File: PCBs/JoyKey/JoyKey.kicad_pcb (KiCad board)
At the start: 2 copper layers, 97 x 56.8 mm, 50 parts, among them J1 OLED_DISPLAY, J2 Conn_01x03_Socket, J3 Testpad wire hole1, J4 JST PH, J5 Top Trigger 1, J6 Top Trigger 2, Q1 PMOS,Si7157DP, SW1 RotaryEncoder_Switch, SW2 SW_Push_45deg, SW3 SW_Push_45deg, SW4 SW_Push_45deg, SW5 SW_Push_45deg, SW6 SW_Push_45deg, SW7 SW_Push_45deg, U1 BQ25060, U3 XIAO-RP2040-DIP, U4 LP2981-3.3, U5 2_axis_analog_joystick_button

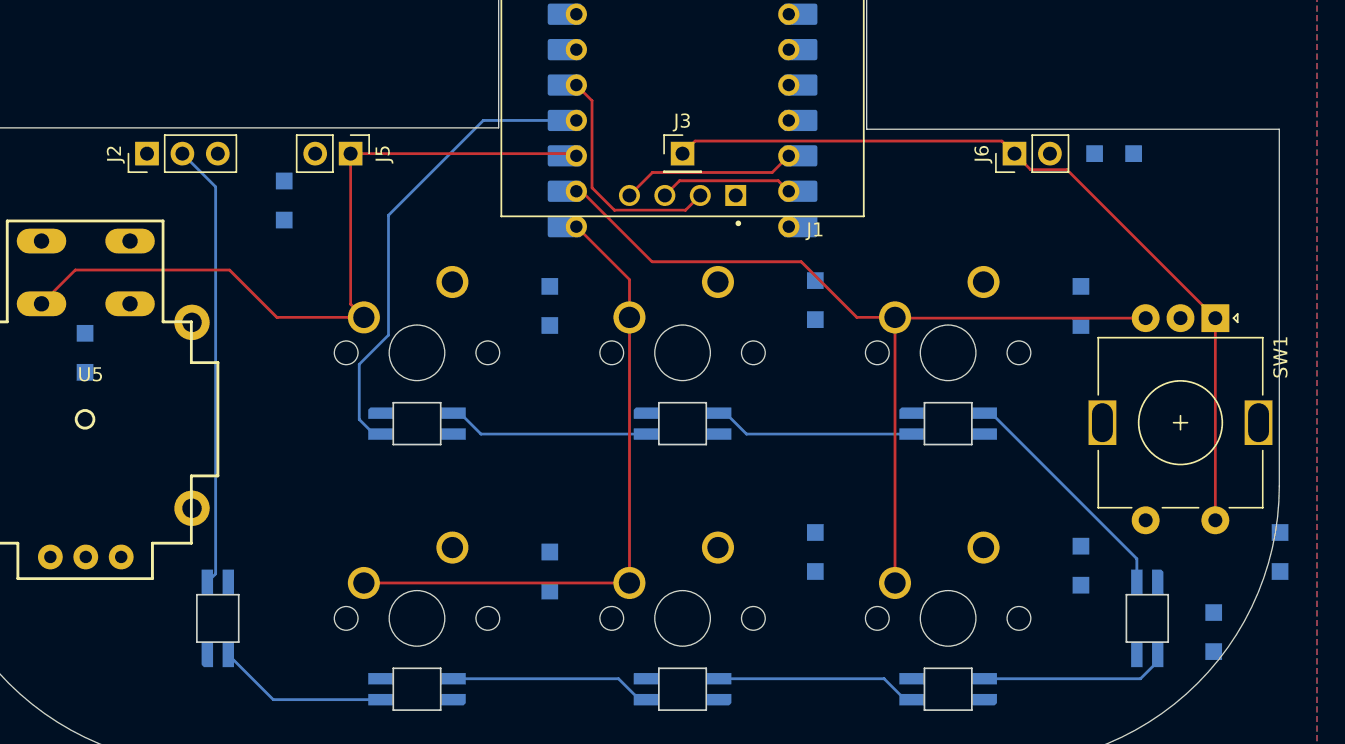
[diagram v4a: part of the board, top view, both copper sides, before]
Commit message: Finished Row routing
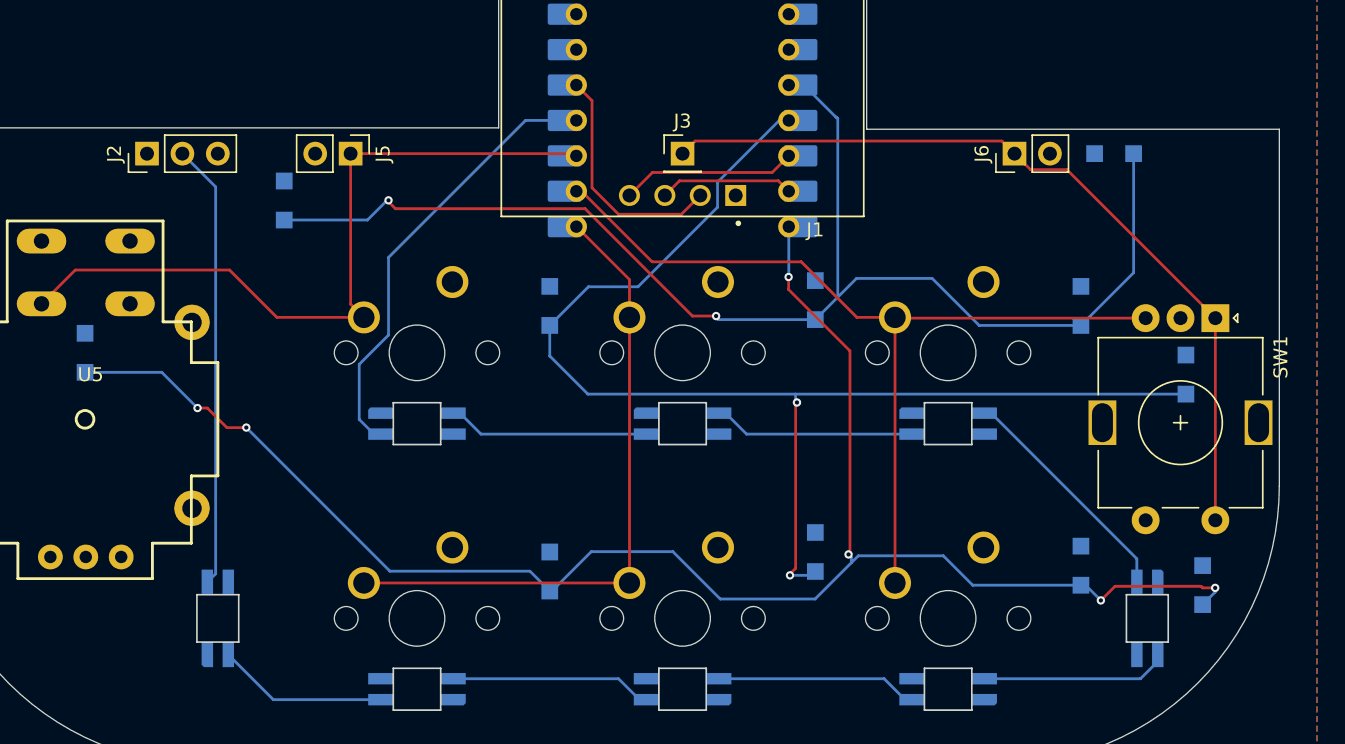
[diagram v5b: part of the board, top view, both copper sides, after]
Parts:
- moved D12 14.4 mm to (176.6, 111.1)
- moved D17 3.46 mm to (177.8, 126.2)
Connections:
- U3 pad 3: /ROW1 -> /ROW0
- U3 pad 4: /ROW2 -> /ROW1
- U3 pad 7: /ROW0 -> /ROW2
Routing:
- net /ROW2: track 0.00 -> 121.1 mm, vias 0 -> 6
- net /ROW0: track 0.00 -> 95.2 mm, vias 0 -> 2
- net /ROW1: track 0.00 -> 88.4 mm, vias 0 -> 2
- net /WS2812B: track 32.9 -> 31.2 mm

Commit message: Add Mating point GND to encoder
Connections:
- SW1 pad MP: (no net) -> GND
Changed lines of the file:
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@@
 			(layers "*.Cu" "*.Mask")
 			(remove_unused_layers no)
+			(net 7 "GND")
+			(pinfunction "MP")
+			(pintype "input")
 		)
 		(pad "MP" thru_hole rect
@@
 			(layers "*.Cu" "*.Mask")
 			(remove_unused_layers no)
+			(net 7 "GND")
+			(pinfunction "MP")
+			(pintype "input")
 		)
 		(pad "S1" thru_hole circle

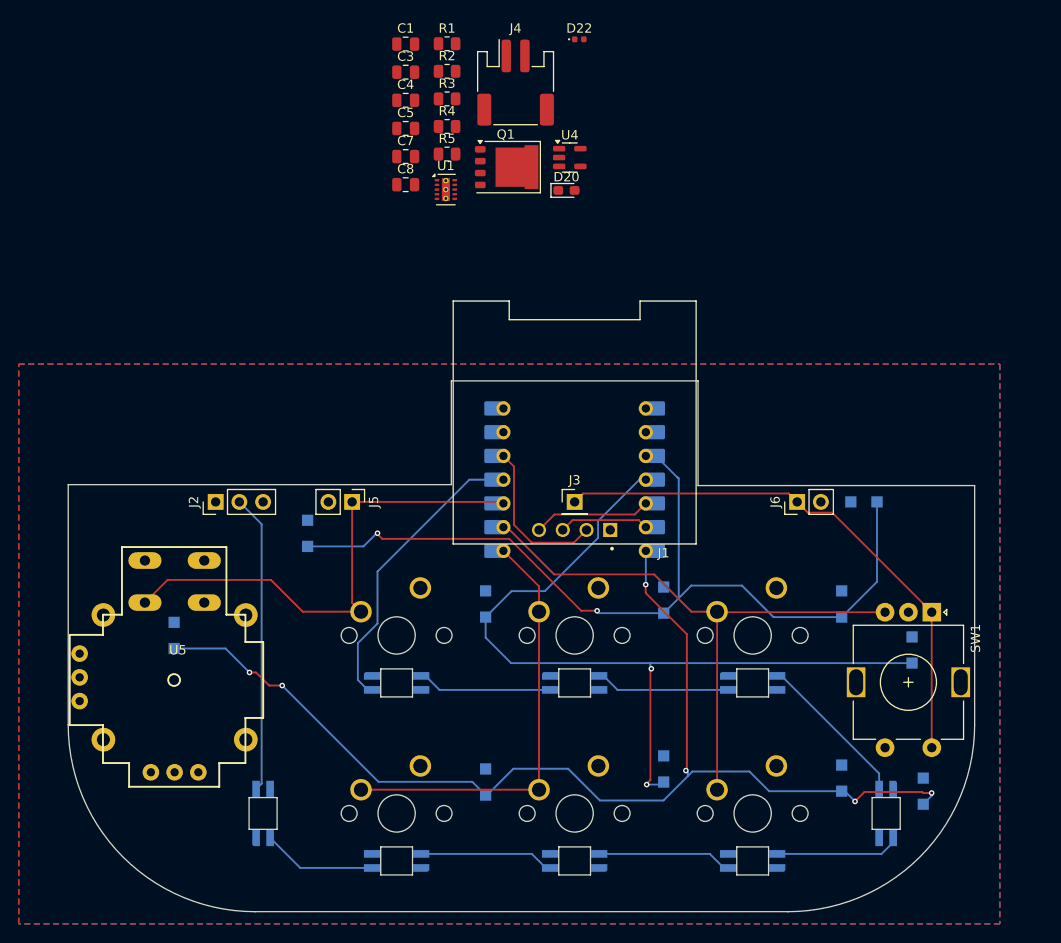
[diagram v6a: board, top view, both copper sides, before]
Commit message: Finished 3v3 and Diode routing
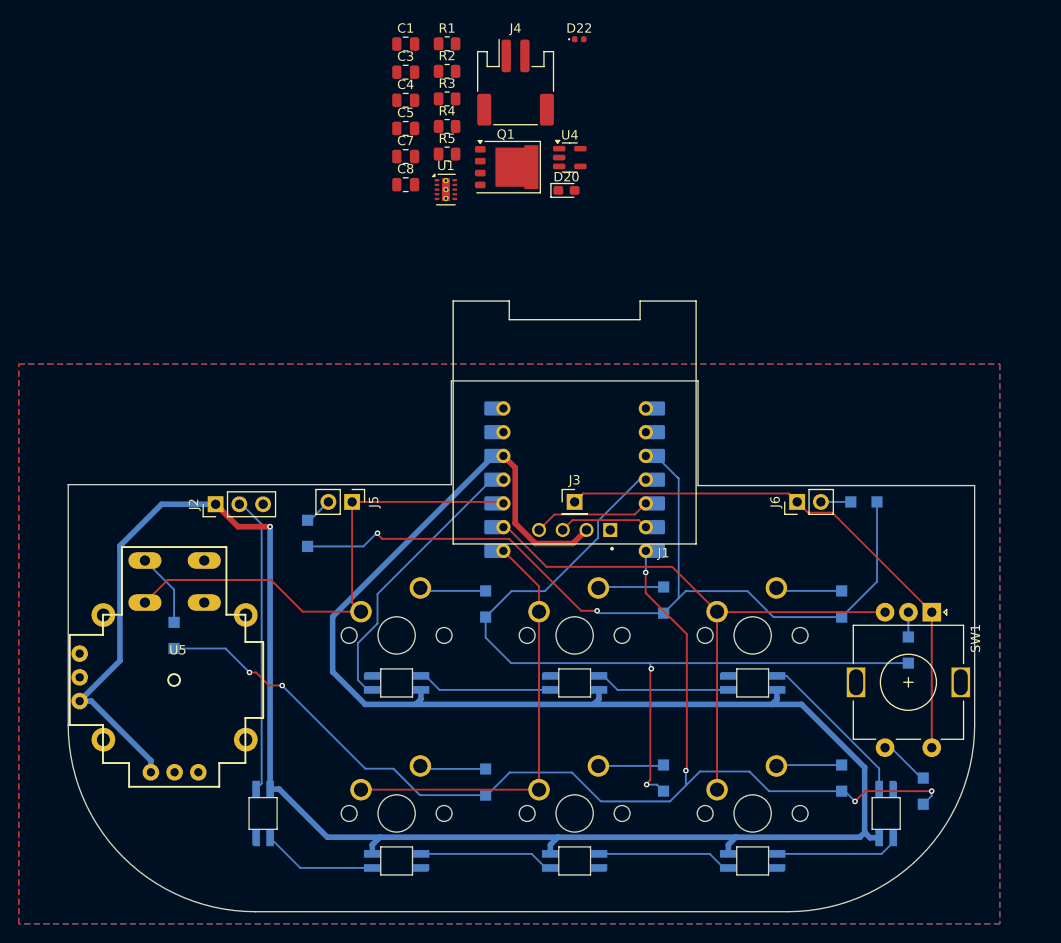
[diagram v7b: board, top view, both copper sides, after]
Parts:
- moved D11 0.98 mm to (150.0, 124.8)
- moved D12 0.40 mm to (176.2, 111.1)
- moved J2 0.25 mm to (102.1, 95.5)
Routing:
- net +3V3: track 16.9 -> 272.6 mm, vias 0 -> 1
- net /Analog Input/StickButtonB: track 0.00 -> 7.91 mm
- net Net-(D9-A): track 0.00 -> 7.12 mm
- net Net-(D15-A): track 0.00 -> 7.12 mm
- net Net-(D3-A): track 0.00 -> 7.12 mm
- net Net-(D2-A): track 0.00 -> 7.03 mm
- net Net-(D16-A): track 0.00 -> 7.03 mm
- net Net-(D11-A): track 0.00 -> 7.01 mm
- net /Analog Input/EC11SWB: track 0.00 -> 5.43 mm
- net Net-(D4-A): track 0.00 -> 3.20 mm
- net Net-(D1-A): track 0.00 -> 3.04 mm
- net /Analog Input/EC11Common: track 0.00 -> 2.66 mm
- net /WS2812B: track 31.2 -> 29.8 mm
- net /ROW2: track 121.1 -> 121.9 mm

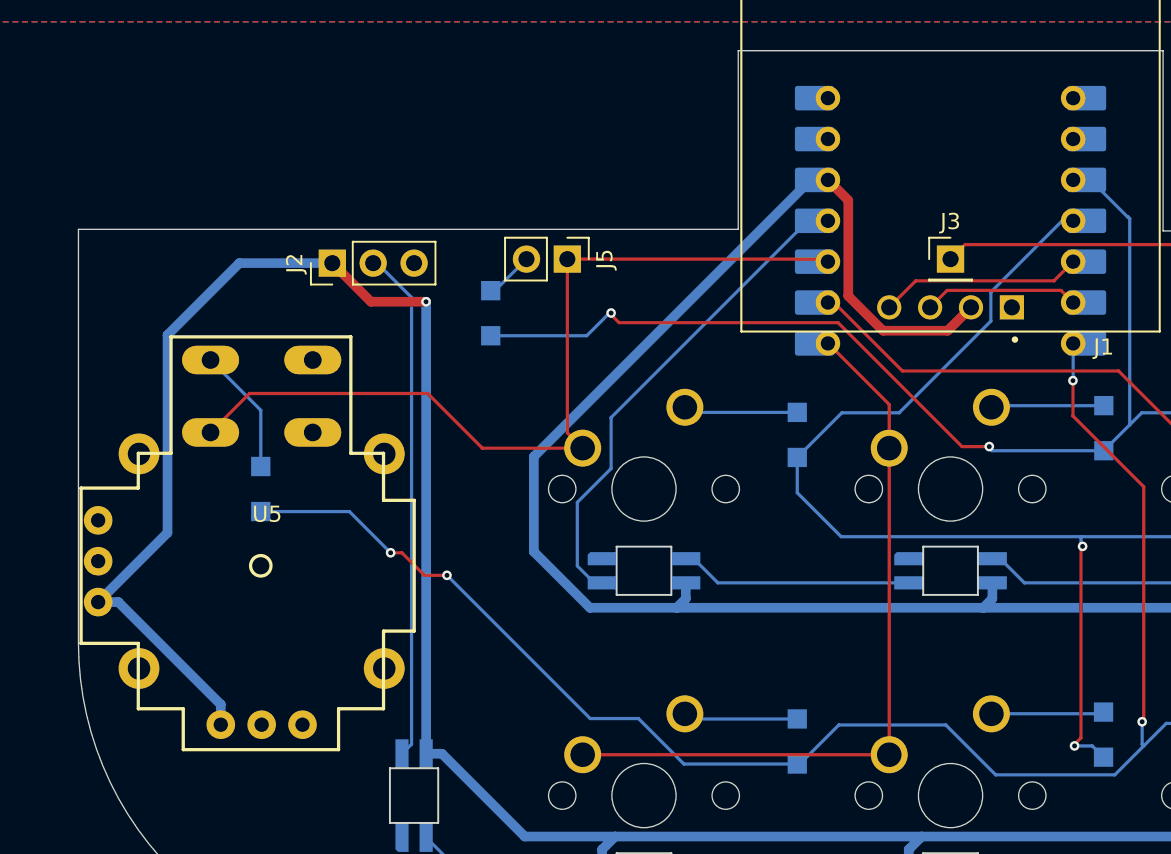
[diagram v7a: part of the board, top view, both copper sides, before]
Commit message: Finished Joystick Routing
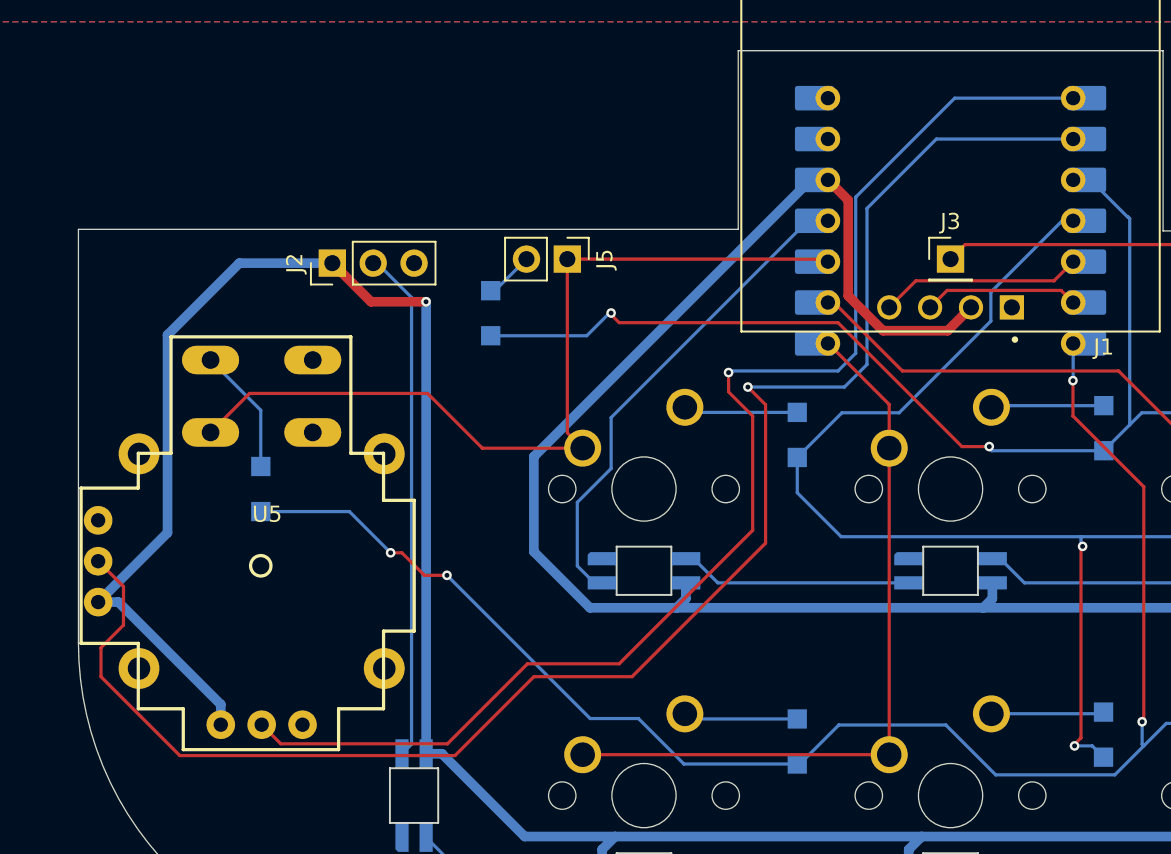
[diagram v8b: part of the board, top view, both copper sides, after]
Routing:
- net /JoystickY: track 0.00 -> 99.6 mm, vias 0 -> 1
- net /JoystickX: track 0.00 -> 81.1 mm, vias 0 -> 1
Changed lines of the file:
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@@
+	)
+	(segment
+		(start 109.228623 125.371377)
+		(end 114.2 120.4)
+		(width 0.2)
+		(layer "F.Cu")
+		(net 32)
+	)
+	(segment
+		(start 97.685327 124.182377)
+		(end 98.874327 125.371377)
+		(width 0.2)
+		(layer "F.Cu")
+		(net 32)
+	)
+	(segment
+		(start 126.7 103.5)
+		(end 126.7 102.3)
+		(width 0.2)
+		(layer "F.Cu")
+		(net 32)
+	)
+	(segment
+		(start 128.2 105)
+		(end 126.7 103.5)
+		(width 0.2)
+		(layer "F.Cu")
+		(net 32)
+	)
+	(segment
+		(start 128.2 112.1)
+		(end 128.2 105)
+		(width 0.2)
+		(layer "F.Cu")
+		(net 32)
+	)
+	(segment
+		(start 114.2 120.4)
+		(end 119.9 120.4)
+		(width 0.2)
+		(layer "F.Cu")
+		(net 32)
+	)
+	(segment
+		(start 119.9 120.4)
+		(end 128.2 112.1)
+		(width 0.2)
+		(layer "F.Cu")
+		(net 32)
+	)
+	(segment
+		(start 98.874327 125.371377)
+		(end 109.228623 125.371377)
+		(width 0.2)
+		(layer "F.Cu")
+		(net 32)
+	)
+	(via
+		(at 126.7 102.3)
+		(size 0.6)
+		(drill 0.3)
+		(layers "F.Cu" "B.Cu")
+		(net 32)
+	)
+	(segment
+		(start 134.6 101.1)
+		(end 133.5 102.2)
+		(width 0.2)
+		(layer "B.Cu")
+		(net 32)
+	)
+	(segment
+		(start 148.11375 85.24875)
+		(end 140.75125 85.24875)
+		(width 0.2)
+		(layer "B.Cu")
+		(net 32)
+	)
+	(segment
+		(start 140.75125 85.24875)
+		(end 134.6 91.4)
+		(width 0.2)
+		(layer "B.Cu")
+		(net 32)
+	)
+	(segment
+		(start 134.6 91.4)
+		(end 134.6 101.1)
+		(width 0.2)
+		(layer "B.Cu")
+		(net 32)
+	)
+	(segment
+		(start 133.5 102.2)
+		(end 126.8 102.2)
+		(width 0.2)
+		(layer "B.Cu")
+		(net 32)
+	)
+	(segment
+		(start 126.8 102.2)
+		(end 126.7 102.3)
+		(width 0.2)
+		(layer "B.Cu")
+		(net 32)
 	)
 	(segment
@@
 	)
 	(segment
+		(start 129 112.9)
+		(end 120.7 121.2)
+		(width 0.2)
+		(layer "F.Cu")
+		(net 37)
+	)
+	(segment
+		(start 92.6 126.1)
+		(end 87.7 121.2)
+		(width 0.2)
+		(layer "F.Cu")
+		(net 37)
+	)
+	(segment
+		(start 87.7 121.2)
+		(end 87.7 119.4)
+		(width 0.2)
+		(layer "F.Cu")
+		(net 37)
+	)
+	(segment
+		(start 127.9 103.2)
+		(end 129 104.3)
+		(width 0.2)
+		(layer "F.Cu")
+		(net 37)
+	)
+	(segment
+		(start 109.7 126.1)
+		(end 92.6 126.1)
+		(width 0.2)
+		(layer "F.Cu")
+		(net 37)
+	)
+	(segment
+		(start 87.7 119.4)
+		(end 89.1 118)
+		(width 0.2)
+		(layer "F.Cu")
+		(net 37)
+	)
+	(segment
+		(start 120.7 121.2)
+		(end 114.6 121.2)
+		(width 0.2)
+		(layer "F.Cu")
+		(net 37)
+	)
+	(segment
+		(start 129 104.3)
+		(end 129 112.9)
+		(width 0.2)
+		(layer "F.Cu")
+		(net 37)
+	)
+	(segment
+		(start 89.1 115.59705)
+		(end 87.525327 114.022377)
+		(width 0.2)
+		(layer "F.Cu")
+		(net 37)
+	)
+	(segment
+		(start 114.6 121.2)
+		(end 109.7 126.1)
+		(width 0.2)
+		(layer "F.Cu")
+		(net 37)
+	)
+	(segment
+		(start 89.1 118)
+		(end 89.1 115.59705)
+		(width 0.2)
+		(layer "F.Cu")
+		(net 37)
+	)
+	(via
+		(at 127.9 103.2)
+		(size 0.6)
+		(drill 0.3)
+		(layers "F.Cu" "B.Cu")
+		(net 37)
+	)
+	(segment
+		(start 135.3 101.8)
+		(end 133.9 103.2)
+		(width 0.2)
+		(layer "B.Cu")
+		(net 37)
+	)
+	(segment
+		(start 135.3 92.1)
+		(end 135.3 101.8)
+		(width 0.2)
+		(layer "B.Cu")
+		(net 37)
+	)
+	(segment
+		(start 133.9 103.2)
+		(end 127.9 103.2)
+		(width 0.2)
+		(layer "B.Cu")
+		(net 37)
+	)
+	(segment
+		(start 148.11375 87.78875)
+		(end 139.61125 87.78875)
+		(width 0.2)
+		(layer "B.Cu")
+		(net 37)
+	)
+	(segment
+		(start 139.61125 87.78875)
+		(end 135.3 92.1)
+		(width 0.2)
+		(layer "B.Cu")
+		(net 37)
+	)
+	(segment
